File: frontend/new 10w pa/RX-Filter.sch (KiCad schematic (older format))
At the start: 95 parts, among them Q4 2N7000, U3 74LS145

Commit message: BOM and PCB updates
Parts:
- added C86: 150pF, HERMESLITE:C_0805, symbol C
- C58: value 300pF -> 150pF
- L40: value 4700uH -> 4700nH
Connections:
- net at C44.1, C69.1, D5.2 (K)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: no longer U3.7 (Q6)
- net at C45.1, C70.1, D4.2 (K)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: now also U3.7 (Q6)
- net at C58.1, C64.1, D11.2 (K)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: now also C86.1
- net at C58.2, L24.2: now also C86.2
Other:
- moved on the sheet: C59, L29
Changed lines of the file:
@@
 P 6100 6300
 F 0 "C58" V 6050 6350 40  0000 L CNN
-F 1 "300pF" V 6050 6100 40  0000 L CNN
+F 1 "150pF" V 6050 6100 40  0000 L CNN
 F 2 "HERMESLITE:C_0805" H 6138 6150 30  0001 C CNN
 F 3 "" H 6100 6300 60  0000 C CNN
@@
 L INDUCTOR L29
 U 1 1 54A2CBAA
-P 6300 6600
-F 0 "L29" V 6250 6600 40  0000 C CNN
-F 1 "1.5uH" V 6400 6600 40  0000 C CNN
-F 2 "HERMESLITE:Choke_SMD_1206_Standard" H 6300 6600 60  0001 C CNN
-F 3 "" H 6300 6600 60  0000 C CNN
-	1    6300 6600
+P 6350 6600
+F 0 "L29" V 6300 6600 40  0000 C CNN
+F 1 "1.5uH" V 6450 6600 40  0000 C CNN
+F 2 "HERMESLITE:Choke_SMD_1206_Standard" H 6350 6600 60  0001 C CNN
+F 3 "" H 6350 6600 60  0000 C CNN
+	1    6350 6600
 	1    0    0    -1
 $EndComp
@@
 L C C59
 U 1 1 54A2CBDB
-P 6500 7000
-F 0 "C59" V 6450 7100 40  0000 L CNN
-F 1 "0.01uF" V 6650 6900 40  0000 L CNN
-F 2 "HERMESLITE:C_0805" H 6538 6850 30  0001 C CNN
-F 3 "" H 6500 7000 60  0000 C CNN
-	1    6500 7000
+P 6600 7000
+F 0 "C59" V 6550 7100 40  0000 L CNN
+F 1 "0.01uF" V 6750 6900 40  0000 L CNN
+F 2 "HERMESLITE:C_0805" H 6638 6850 30  0001 C CNN
+F 3 "" H 6600 7000 60  0000 C CNN
+	1    6600 7000
 	0    -1   -1   0
 $EndComp
@@
 L GND #PWR071
 U 1 1 54A2CBE7
-P 6700 7000
-F 0 "#PWR071" H 6700 7000 30  0001 C CNN
-F 1 "GND" H 6700 6930 30  0001 C CNN
-F 2 "" H 6700 7000 50  0000 C CNN
-F 3 "" H 6700 7000 50  0000 C CNN
-	1    6700 7000
+P 6800 7000
+F 0 "#PWR071" H 6800 7000 30  0001 C CNN
+F 1 "GND" H 6800 6930 30  0001 C CNN
+F 2 "" H 6800 7000 50  0000 C CNN
+F 3 "" H 6800 7000 50  0000 C CNN
+	1    6800 7000
 	0    -1   -1   0
 $EndComp
@@
 	6300 6300 6550 6300
 Wire Wire Line
-	5050 7000 6300 7000
-Wire Wire Line
-	6300 7000 6300 6900
+	5050 7000 6400 7000
 Wire Wire Line
 	8350 6300 6950 6300
@@
 P 7500 1700
 F 0 "L40" V 7450 1700 40  0000 C CNN
-F 1 "4700uH" V 7600 1700 40  0000 C CNN
+F 1 "4700nH" V 7600 1700 40  0000 C CNN
 F 2 "HERMESLITE:Choke_SMD_1206_Standard" H 7500 1700 60  0001 C CNN
 F 3 "" H 7500 1700 60  0000 C CNN
@@
 	2800 3600 2200 3600
 Wire Wire Line
-	2900 2700 2900 3500
-Wire Wire Line
-	2900 3500 2200 3500
-Wire Wire Line
-	2300 3200 2300 3500
-Wire Wire Line
 	2300 3200 2200 3200
-Connection ~ 2300 3500
 Wire Wire Line
 	2200 3300 2300 3300
 Connection ~ 2300 3300
 Wire Wire Line
-	2200 3400 2300 3400
+	2900 3400 2200 3400
 Connection ~ 2300 3400
 Wire Wire Line
@@
 	1    0    0    -1
 $EndComp
+Wire Wire Line
+	2300 3200 2300 3400
+Wire Wire Line
+	2900 2700 2900 3400
+Wire Wire Line
+	2300 3600 2300 3500
+Connection ~ 2300 3600
+Wire Wire Line
+	2300 3500 2200 3500
+Wire Wire Line
+	6350 6900 6350 7000
+Connection ~ 6350 7000
+$Comp
+L C C86
+U 1 1 54C9395B
+P 6100 6500
+F 0 "C86" V 6050 6550 40  0000 L CNN
+F 1 "150pF" V 6050 6300 40  0000 L CNN
+F 2 "HERMESLITE:C_0805" H 6138 6350 30  0001 C CNN
+F 3 "" H 6100 6500 60  0000 C CNN
+	1    6100 6500
+	0    1    1    0
+$EndComp
+Wire Wire Line
+	5900 6300 5900 6500
+Wire Wire Line
+	6300 6300 6300 6500
+Connection ~ 6350 6300
 $EndSCHEMATC

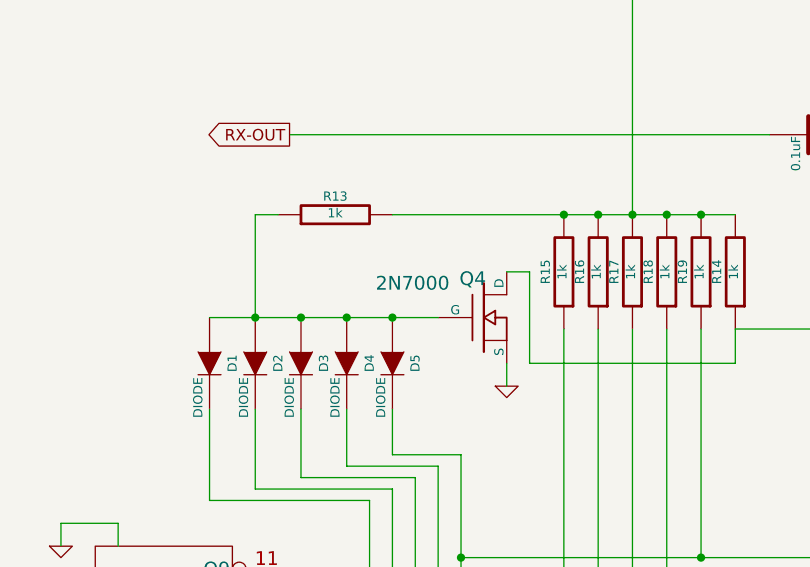
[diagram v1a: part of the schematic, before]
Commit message: PTT change
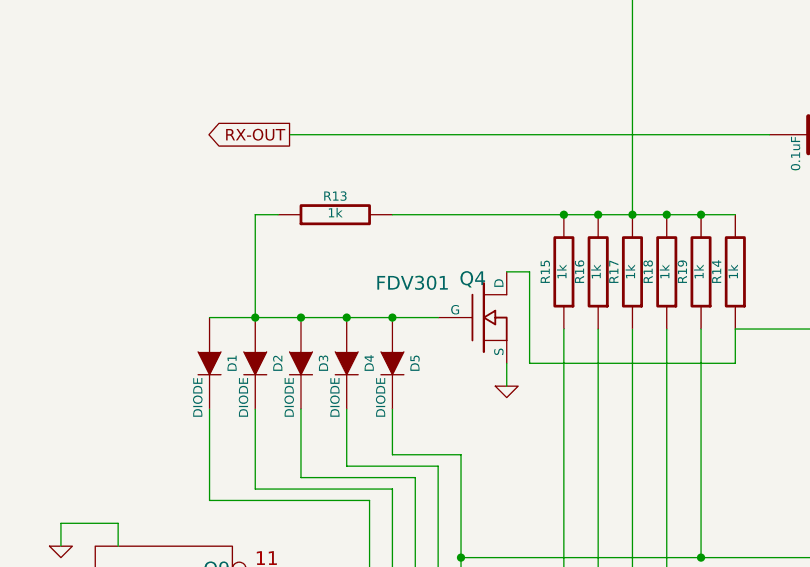
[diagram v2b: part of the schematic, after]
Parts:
- Q4: value 2N7000 -> FDV301
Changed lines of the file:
@@
 encoding utf-8
 Sheet 3 3
-Title "Hermes Lite Basic RX Filters"
-Date "21 January 2015"
-Rev "1.2"
+Title "Hermes Lite RX Filters"
+Date "03 February 2015"
+Rev "1.21"
 Comp "SofterHardware"
-Comment1 "AC9HY"
+Comment1 "AC9HY/WA2EUJ"
 Comment2 ""
 Comment3 ""
@@
 $EndComp
 $Comp
-L GND #PWR044
+L GND #PWR045
 U 1 1 54A26D4B
 P 7800 2700
-F 0 "#PWR044" H 7800 2700 30  0001 C CNN
+F 0 "#PWR045" H 7800 2700 30  0001 C CNN
 F 1 "GND" H 7800 2630 30  0001 C CNN
 F 2 "" H 7800 2700 50  0000 C CNN
@@
 $EndComp
 $Comp
-L GND #PWR045
+L GND #PWR046
 U 1 1 54A26D51
 P 6550 2700
-F 0 "#PWR045" H 6550 2700 30  0001 C CNN
+F 0 "#PWR046" H 6550 2700 30  0001 C CNN
 F 1 "GND" H 6550 2630 30  0001 C CNN
 F 2 "" H 6550 2700 50  0000 C CNN
@@
 $EndComp
 $Comp
-L GND #PWR046
+L GND #PWR047
 U 1 1 54A26D57
 P 6300 2900
-F 0 "#PWR046" H 6300 2900 30  0001 C CNN
+F 0 "#PWR047" H 6300 2900 30  0001 C CNN
 F 1 "GND" H 6300 2830 30  0001 C CNN
 F 2 "" H 6300 2900 50  0000 C CNN
@@
 $EndComp
 $Comp
-L GND #PWR047
+L GND #PWR048
 U 1 1 54A26D5D
 P 5300 2700
-F 0 "#PWR047" H 5300 2700 30  0001 C CNN
+F 0 "#PWR048" H 5300 2700 30  0001 C CNN
 F 1 "GND" H 5300 2630 30  0001 C CNN
 F 2 "" H 5300 2700 50  0000 C CNN
@@
 $EndComp
 $Comp
-L GND #PWR048
+L GND #PWR049
 U 1 1 54A26D72
 P 4650 3000
-F 0 "#PWR048" H 4650 3000 30  0001 C CNN
+F 0 "#PWR049" H 4650 3000 30  0001 C CNN
 F 1 "GND" H 4650 2930 30  0001 C CNN
 F 2 "" H 4650 3000 50  0000 C CNN
@@
 $EndComp
 $Comp
-L GND #PWR049
+L GND #PWR050
 U 1 1 54A26D78
 P 7950 3000
-F 0 "#PWR049" H 7950 3000 30  0001 C CNN
+F 0 "#PWR050" H 7950 3000 30  0001 C CNN
 F 1 "GND" H 7950 2930 30  0001 C CNN
 F 2 "" H 7950 3000 50  0000 C CNN
@@
 $EndComp
 $Comp
-L GND #PWR050
+L GND #PWR051
 U 1 1 54A28AFC
 P 7800 4700
-F 0 "#PWR050" H 7800 4700 30  0001 C CNN
+F 0 "#PWR051" H 7800 4700 30  0001 C CNN
 F 1 "GND" H 7800 4630 30  0001 C CNN
 F 2 "" H 7800 4700 50  0000 C CNN
@@
 $EndComp
 $Comp
-L GND #PWR051
+L GND #PWR052
 U 1 1 54A28B02
 P 6550 4700
-F 0 "#PWR051" H 6550 4700 30  0001 C CNN
+F 0 "#PWR052" H 6550 4700 30  0001 C CNN
 F 1 "GND" H 6550 4630 30  0001 C CNN
 F 2 "" H 6550 4700 50  0000 C CNN
@@
 $EndComp
 $Comp
-L GND #PWR052
+L GND #PWR053
 U 1 1 54A28B08
 P 6300 4900
-F 0 "#PWR052" H 6300 4900 30  0001 C CNN
+F 0 "#PWR053" H 6300 4900 30  0001 C CNN
 F 1 "GND" H 6300 4830 30  0001 C CNN
 F 2 "" H 6300 4900 50  0000 C CNN
@@
 $EndComp
 $Comp
-L GND #PWR053
+L GND #PWR054
 U 1 1 54A28B0E
 P 5300 4700
-F 0 "#PWR053" H 5300 4700 30  0001 C CNN
+F 0 "#PWR054" H 5300 4700 30  0001 C CNN
 F 1 "GND" H 5300 4630 30  0001 C CNN
 F 2 "" H 5300 4700 50  0000 C CNN
@@
 $EndComp
 $Comp
-L GND #PWR054
+L GND #PWR055
 U 1 1 54A28B21
 P 4650 5000
-F 0 "#PWR054" H 4650 5000 30  0001 C CNN
+F 0 "#PWR055" H 4650 5000 30  0001 C CNN
 F 1 "GND" H 4650 4930 30  0001 C CNN
 F 2 "" H 4650 5000 50  0000 C CNN
@@
 $EndComp
 $Comp
-L GND #PWR055
+L GND #PWR056
 U 1 1 54A28B27
 P 7950 5000
-F 0 "#PWR055" H 7950 5000 30  0001 C CNN
+F 0 "#PWR056" H 7950 5000 30  0001 C CNN
 F 1 "GND" H 7950 4930 30  0001 C CNN
 F 2 "" H 7950 5000 50  0000 C CNN
@@
 $EndComp
 $Comp
-L GND #PWR056
+L GND #PWR057
 U 1 1 54A2A84A
 P 7800 3700
-F 0 "#PWR056" H 7800 3700 30  0001 C CNN
+F 0 "#PWR057" H 7800 3700 30  0001 C CNN
 F 1 "GND" H 7800 3630 30  0001 C CNN
 F 2 "" H 7800 3700 50  0000 C CNN
@@
 $EndComp
 $Comp
-L GND #PWR057
+L GND #PWR058
 U 1 1 54A2A850
 P 6550 3700
-F 0 "#PWR057" H 6550 3700 30  0001 C CNN
+F 0 "#PWR058" H 6550 3700 30  0001 C CNN
 F 1 "GND" H 6550 3630 30  0001 C CNN
 F 2 "" H 6550 3700 50  0000 C CNN
@@
 $EndComp
 $Comp
-L GND #PWR058
+L GND #PWR059
 U 1 1 54A2A856
 P 6300 3900
-F 0 "#PWR058" H 6300 3900 30  0001 C CNN
+F 0 "#PWR059" H 6300 3900 30  0001 C CNN
 F 1 "GND" H 6300 3830 30  0001 C CNN
 F 2 "" H 6300 3900 50  0000 C CNN
@@
 $EndComp
 $Comp
-L GND #PWR059
+L GND #PWR060
 U 1 1 54A2A85C
 P 5300 3700
-F 0 "#PWR059" H 5300 3700 30  0001 C CNN
+F 0 "#PWR060" H 5300 3700 30  0001 C CNN
 F 1 "GND" H 5300 3630 30  0001 C CNN
 F 2 "" H 5300 3700 50  0000 C CNN
@@
 $EndComp
 $Comp
-L GND #PWR060
+L GND #PWR061
 U 1 1 54A2A86F
 P 4650 4000
-F 0 "#PWR060" H 4650 4000 30  0001 C CNN
+F 0 "#PWR061" H 4650 4000 30  0001 C CNN
 F 1 "GND" H 4650 3930 30  0001 C CNN
 F 2 "" H 4650 4000 50  0000 C CNN
@@
 $EndComp
 $Comp
-L GND #PWR061
+L GND #PWR062
 U 1 1 54A2A875
 P 7950 4000
-F 0 "#PWR061" H 7950 4000 30  0001 C CNN
+F 0 "#PWR062" H 7950 4000 30  0001 C CNN
 F 1 "GND" H 7950 3930 30  0001 C CNN
 F 2 "" H 7950 4000 50  0000 C CNN
@@
 $EndComp
 $Comp
-L GND #PWR062
+L GND #PWR063
 U 1 1 54A2AFAC
 P 7800 5700
-F 0 "#PWR062" H 7800 5700 30  0001 C CNN
+F 0 "#PWR063" H 7800 5700 30  0001 C CNN
 F 1 "GND" H 7800 5630 30  0001 C CNN
 F 2 "" H 7800 5700 50  0000 C CNN
@@
 $EndComp
 $Comp
-L GND #PWR063
+L GND #PWR064
 U 1 1 54A2AFB2
 P 6550 5700
-F 0 "#PWR063" H 6550 5700 30  0001 C CNN
+F 0 "#PWR064" H 6550 5700 30  0001 C CNN
 F 1 "GND" H 6550 5630 30  0001 C CNN
 F 2 "" H 6550 5700 50  0000 C CNN
@@
 $EndComp
 $Comp
-L GND #PWR064
+L GND #PWR065
 U 1 1 54A2AFB8
 P 6300 5900
-F 0 "#PWR064" H 6300 5900 30  0001 C CNN
+F 0 "#PWR065" H 6300 5900 30  0001 C CNN
 F 1 "GND" H 6300 5830 30  0001 C CNN
 F 2 "" H 6300 5900 50  0000 C CNN
@@
 $EndComp
 $Comp
-L GND #PWR065
+L GND #PWR066
 U 1 1 54A2AFBE
 P 5200 5700
-F 0 "#PWR065" H 5200 5700 30  0001 C CNN
+F 0 "#PWR066" H 5200 5700 30  0001 C CNN
 F 1 "GND" H 5200 5630 30  0001 C CNN
 F 2 "" H 5200 5700 50  0000 C CNN
@@
 $EndComp
 $Comp
-L GND #PWR066
+L GND #PWR067
 U 1 1 54A2AFD1
 P 4600 6000
-F 0 "#PWR066" H 4600 6000 30  0001 C CNN
+F 0 "#PWR067" H 4600 6000 30  0001 C CNN
 F 1 "GND" H 4600 5930 30  0001 C CNN
 F 2 "" H 4600 6000 50  0000 C CNN
@@
 $EndComp
 $Comp
-L GND #PWR067
+L GND #PWR068
 U 1 1 54A2AFD7
 P 8050 6000
-F 0 "#PWR067" H 8050 6000 30  0001 C CNN
+F 0 "#PWR068" H 8050 6000 30  0001 C CNN
 F 1 "GND" H 8050 5930 30  0001 C CNN
 F 2 "" H 8050 6000 50  0000 C CNN
@@
 $EndComp
 $Comp
-L GND #PWR068
+L GND #PWR069
 U 1 1 54A2CBBC
 P 6550 6700
-F 0 "#PWR068" H 6550 6700 30  0001 C CNN
+F 0 "#PWR069" H 6550 6700 30  0001 C CNN
 F 1 "GND" H 6550 6630 30  0001 C CNN
 F 2 "" H 6550 6700 50  0000 C CNN
@@
 $EndComp
 $Comp
-L GND #PWR069
+L GND #PWR070
 U 1 1 54A2CBCE
 P 5300 6700
-F 0 "#PWR069" H 5300 6700 30  0001 C CNN
+F 0 "#PWR070" H 5300 6700 30  0001 C CNN
 F 1 "GND" H 5300 6630 30  0001 C CNN
 F 2 "" H 5300 6700 50  0000 C CNN
@@
 $EndComp
 $Comp
-L GND #PWR070
+L GND #PWR071
 U 1 1 54A2CBE1
 P 4650 7000
-F 0 "#PWR070" H 4650 7000 30  0001 C CNN
+F 0 "#PWR071" H 4650 7000 30  0001 C CNN
 F 1 "GND" H 4650 6930 30  0001 C CNN
 F 2 "" H 4650 7000 50  0000 C CNN
@@
 $EndComp
 $Comp
-L GND #PWR071
+L GND #PWR072
 U 1 1 54A2CBE7
 P 6800 7000
-F 0 "#PWR071" H 6800 7000 30  0001 C CNN
+F 0 "#PWR072" H 6800 7000 30  0001 C CNN
 F 1 "GND" H 6800 6930 30  0001 C CNN
 F 2 "" H 6800 7000 50  0000 C CNN
@@
 Filter Settings for PowerSDR Hermes Ctrl\n(set for RX and TX J16 Pins)\n        1  2  3  4 \nBypass 0  1  0  1 (or higher) \n160M   0  0  0  0\n80M    1  0  0  0\n60M    0  1  0  0\n40M    1  1  0  0\n30M    0  0  1  0\n20M    1  0  1  0\n17M    0  1  1  0\n15M    1  1  1  0\n12M    0  0  0  1\n10M    1  0  0  1
 $Comp
-L GND #PWR072
+L GND #PWR073
 U 1 1 54C1EBE4
 P 1150 3100
-F 0 "#PWR072" H 1150 3100 30  0001 C CNN
+F 0 "#PWR073" H 1150 3100 30  0001 C CNN
 F 1 "GND" H 1150 3030 30  0001 C CNN
 F 2 "" H 1150 3100 50  0000 C CNN
@@
 $EndComp
 $Comp
-L GND #PWR073
+L GND #PWR074
 U 1 1 54C3258A
 P 4900 2000
-F 0 "#PWR073" H 4900 2000 30  0001 C CNN
+F 0 "#PWR074" H 4900 2000 30  0001 C CNN
 F 1 "GND" H 4900 1930 30  0001 C CNN
 F 2 "" H 4900 2000 50  0000 C CNN
@@
 $EndComp
 $Comp
-L GND #PWR074
+L GND #PWR075
 U 1 1 54C32686
 P 7900 2000
-F 0 "#PWR074" H 7900 2000 30  0001 C CNN
+F 0 "#PWR075" H 7900 2000 30  0001 C CNN
 F 1 "GND" H 7900 1930 30  0001 C CNN
 F 2 "" H 7900 2000 50  0000 C CNN
@@
 P 3000 2100
 F 0 "Q4" H 3010 2270 60  0000 R CNN
-F 1 "2N7000" H 2850 2250 60  0000 R CNN
+F 1 "FDV301" H 2850 2250 60  0000 R CNN
 F 2 "SMD_Packages:SOT-23-GDS" H 3000 2100 60  0001 C CNN
 F 3 "" H 3000 2100 60  0000 C CNN
@@
 	3200 1900 3100 1900
 $Comp
-L GND #PWR075
+L GND #PWR076
 U 1 1 54C40367
 P 3100 2400
-F 0 "#PWR075" H 3100 2400 30  0001 C CNN
+F 0 "#PWR076" H 3100 2400 30  0001 C CNN
 F 1 "GND" H 3100 2330 30  0001 C CNN
 F 2 "" H 3100 2400 50  0000 C CNN
